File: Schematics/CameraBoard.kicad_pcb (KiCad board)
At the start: 4 copper layers, 50 x 100 mm, 72 parts, among them J1 Microsemi_FlashPro-JTAG-10, J2 USB_C_Receptacle, U1 STM32F405RGTx, U2 TPS22917DBVR, U3 TPS22917DBVR, U5 AMS1117-3.3, U6 TPS22917DBVR, U8 SN65HVD230, Y1 8mhz

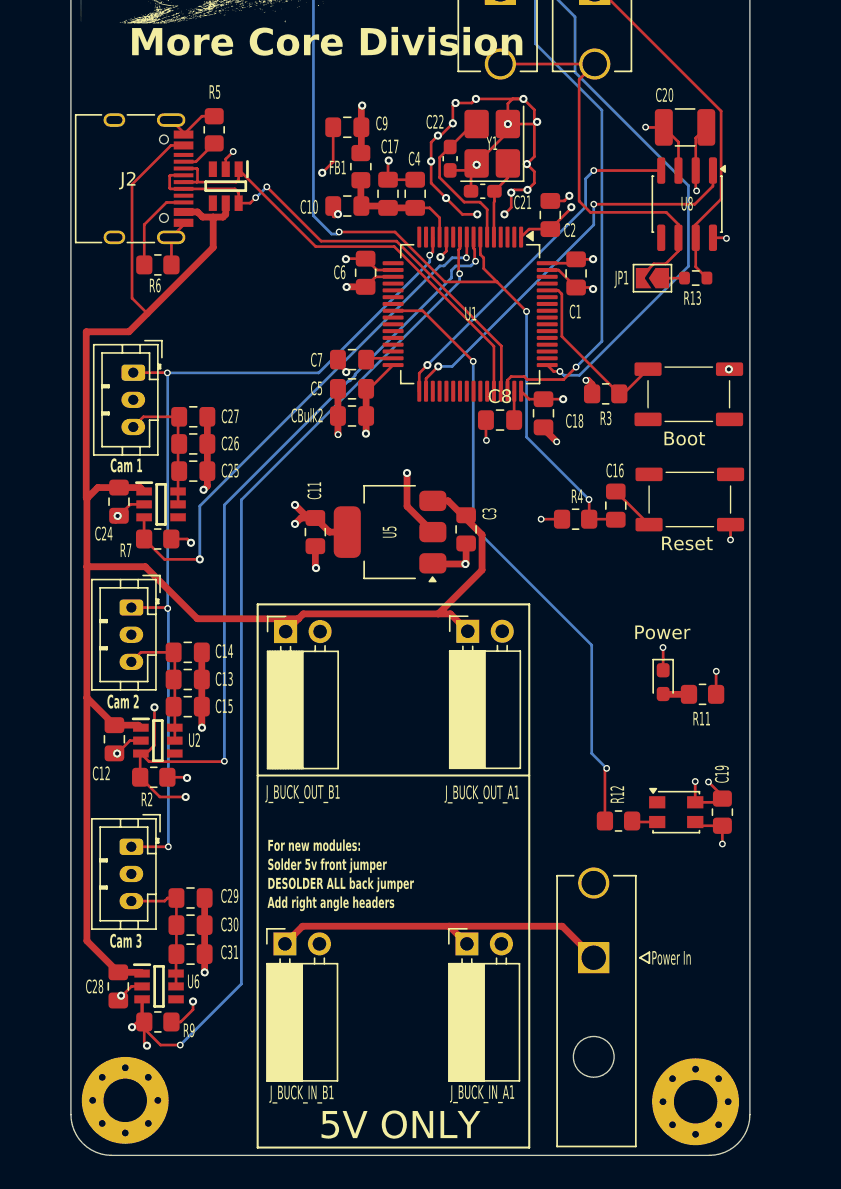
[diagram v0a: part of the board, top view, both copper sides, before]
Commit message: added LCSC numbers and generated BOM, fixed schematic
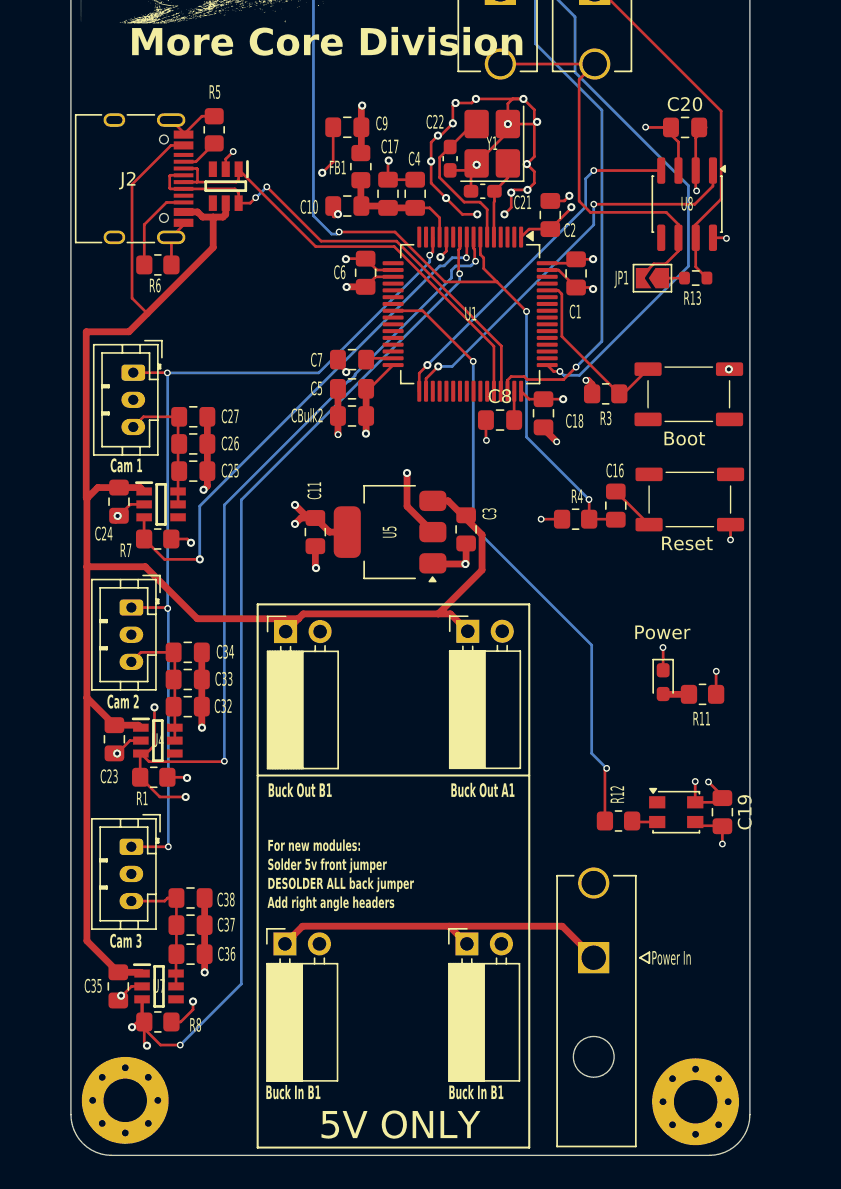
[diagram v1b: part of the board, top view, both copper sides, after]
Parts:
- removed C12, C14, C28, C29: 1u, Capacitor_SMD:C_0805_2012Metric_Pad1.18x1.45mm_HandSolder
- removed C13, C30: 47u, Capacitor_SMD:C_0805_2012Metric_Pad1.18x1.45mm_HandSolder
- removed C15, C31: .1u, Capacitor_SMD:C_0805_2012Metric_Pad1.18x1.45mm_HandSolder
- removed Cam1: Conn_01x03, Connector_JST:JST_PH_B3B-PH-K_1x03_P2.00mm_Vertical
- removed R2, R9: 100k, Resistor_SMD:R_0805_2012Metric_Pad1.20x1.40mm_HandSolder
- removed U2, U6: TPS22917DBVR, myFootprints:SOT95P280X145-6N
- added C23: 1uf, Capacitor_SMD:C_0805_2012Metric_Pad1.18x1.45mm_HandSolder, F.Cu at (74.7, 109.0)
- added C32: 1uf, Capacitor_SMD:C_0805_2012Metric_Pad1.18x1.45mm_HandSolder, F.Cu at (80.0, 106.6)
- added C33: 47uf, Capacitor_SMD:C_0805_2012Metric_Pad1.18x1.45mm_HandSolder, F.Cu at (80.0, 104.6)
- added C34: 100nf, Capacitor_SMD:C_0805_2012Metric_Pad1.18x1.45mm_HandSolder, F.Cu at (80.0, 102.6)
- added C35: 1uf, Capacitor_SMD:C_0805_2012Metric_Pad1.18x1.45mm_HandSolder, F.Cu at (74.9, 127.2)
- added C36: 1uf, Capacitor_SMD:C_0805_2012Metric_Pad1.18x1.45mm_HandSolder, F.Cu at (80.3, 124.8)
- added C37: 47uf, Capacitor_SMD:C_0805_2012Metric_Pad1.18x1.45mm_HandSolder, F.Cu at (80.3, 122.6)
- added C38: 100nf, Capacitor_SMD:C_0805_2012Metric_Pad1.18x1.45mm_HandSolder, F.Cu at (80.3, 120.6)
- added Cam2: Conn_01x03, Connector_JST:JST_PH_B3B-PH-K_1x03_P2.00mm_Vertical, F.Cu at (75.9, 99.3)
- added R1: 100kr, Resistor_SMD:R_0805_2012Metric_Pad1.20x1.40mm_HandSolder, F.Cu at (77.5, 111.8)
- added R8: 100kr, Resistor_SMD:R_0805_2012Metric_Pad1.20x1.40mm_HandSolder, F.Cu at (77.8, 129.8)
- added U4: TPS22917DBVR, myFootprints:SOT95P280X145-6N, F.Cu at (77.8, 109.1)
- added U7: TPS22917DBVR, myFootprints:SOT95P280X145-6N, F.Cu at (77.9, 127.2)
- C11: value 33u -> 33uf
- C17, C3, C9: value 1u -> 1uf
- C19: footprint Resistor_SMD:R_0805_2012Metric_Pad1.20x1.40mm_HandSolder -> Capacitor_SMD:C_0805_2012Metric_Pad1.18x1.45mm_HandSolder
- C20: value 100nF -> 100nf; footprint Capacitor_SMD:C_1210_3225Metric_Pad1.33x2.70mm_HandSolder -> Capacitor_SMD:C_0805_2012Metric_Pad1.18x1.45mm_HandSolder
- C7, C8: value 2.2u -> 2.2uf
- CAN_IN1, CAN_OUT1, PowerIn1: value ~ -> 2 pin Molex
- CBulk2: value 4.7u -> 4.7uf
- R11: value 1k -> 1kr
- R12: value .33k -> 330r
- R13: value 120R -> 120r
- R3: value 100k -> 100kr
- R4: value 10k -> 10kr
- R5, R6: value 5.1k -> 5.1kr
- U1: value STM32F405RGTx -> STM32F405RGT6
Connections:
- U1 pad 10: /Camera_center/CAM_C_PWN_EN -> /MCU/CAM_C_PWN_EN
- U1 pad 8: /Camera_left/CAM_L_PWN_EN -> /MCU/CAM_L_PWN_EN
- U1 pad 9: /Camera_right/CAM_R_PWN_EN -> /MCU/CAM_R_PWN_EN
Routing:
- net /MCU/CAM_L_PWN_EN: track 0.00 -> 63.7 mm, vias 0 -> 4
- net /Camera_left/CAM_L_PWN_EN: track 63.7 -> 0.00 mm, vias 4 -> 0
- net /Camera_right/<NO NET>: track 10.2 -> 20.0 mm
- net /Camera_left/<NO NET>: track 9.81 -> 0.00 mm
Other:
- board text added: "Buck In B1"
- board text added: "Buck Out A1"
- board text added: "Buck Out B1"

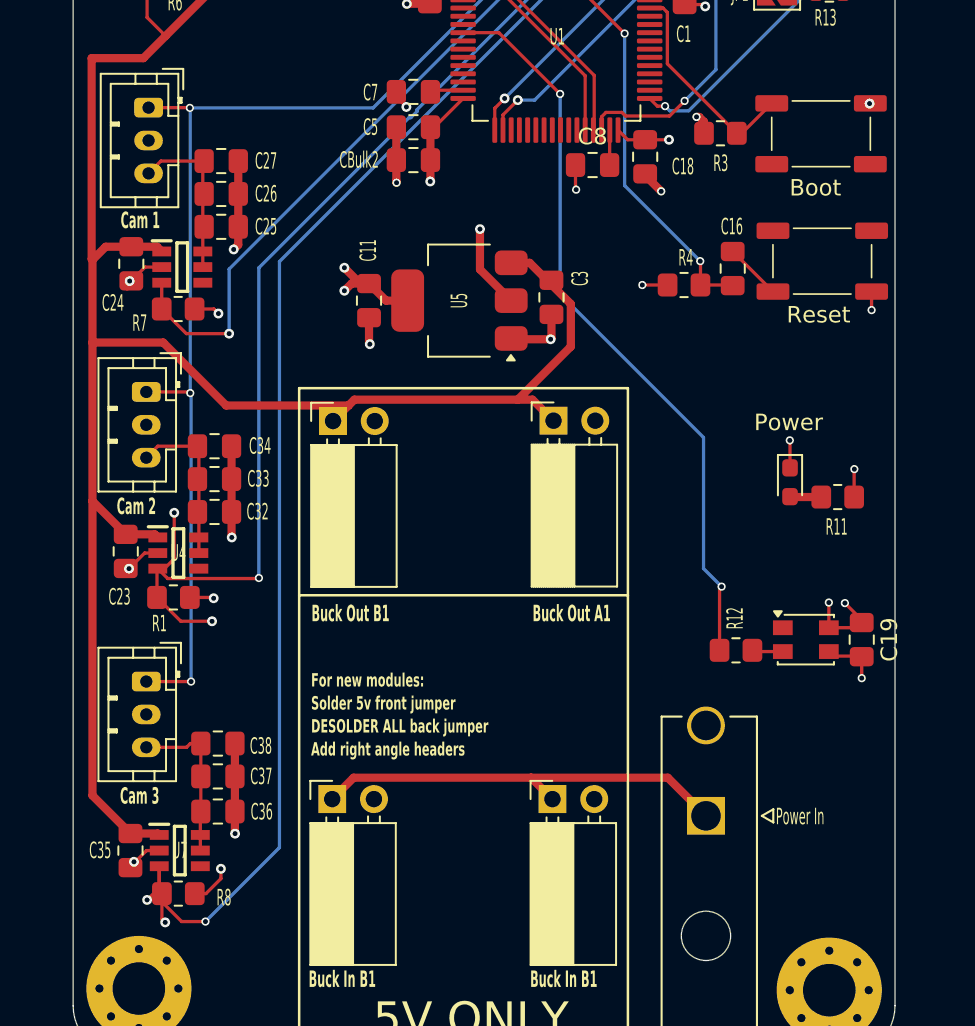
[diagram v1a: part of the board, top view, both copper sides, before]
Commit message: fixed switch layout and unrouted nets
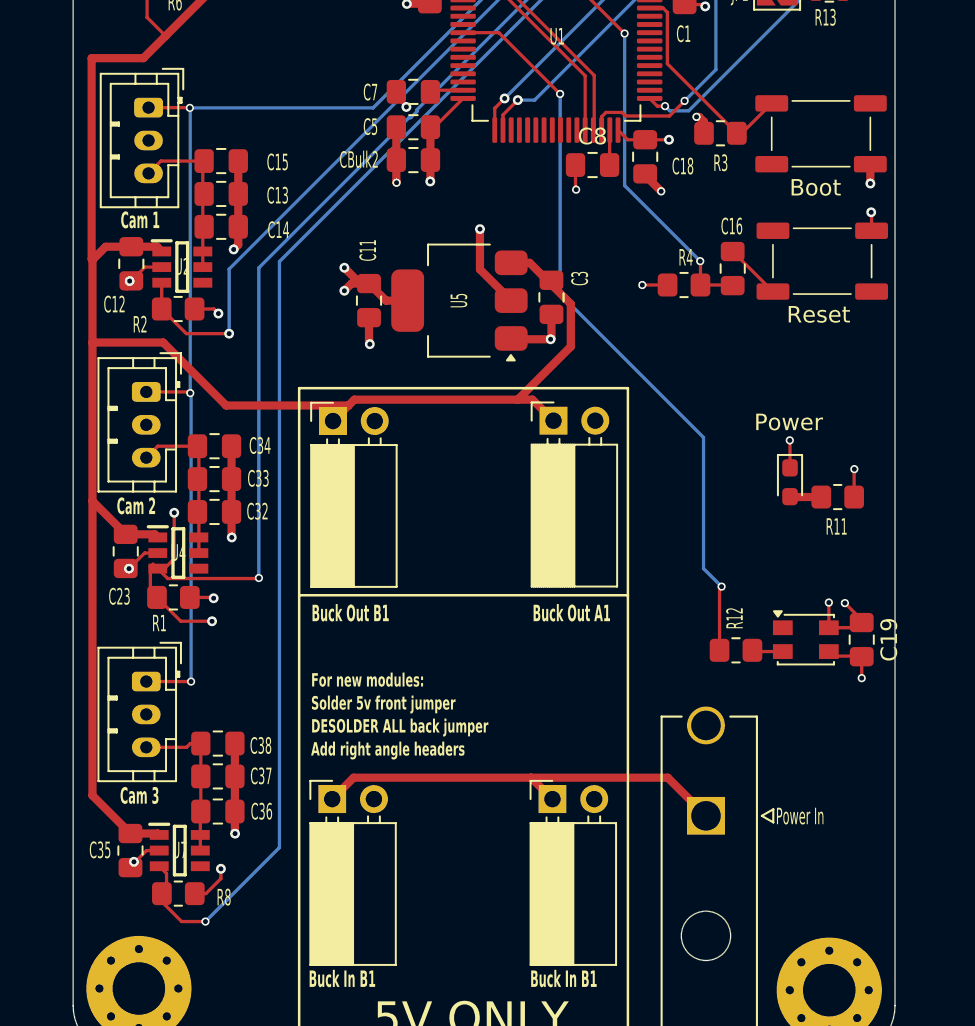
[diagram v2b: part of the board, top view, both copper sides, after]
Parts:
- removed C24, C25: 1u, Capacitor_SMD:C_0805_2012Metric_Pad1.18x1.45mm_HandSolder
- removed C26: 47u, Capacitor_SMD:C_0805_2012Metric_Pad1.18x1.45mm_HandSolder
- removed C27: .1u, Capacitor_SMD:C_0805_2012Metric_Pad1.18x1.45mm_HandSolder
- removed the Cam2 at (76.0, 82.0)
- removed R7: 100k, Resistor_SMD:R_0805_2012Metric_Pad1.20x1.40mm_HandSolder
- removed U3: TPS22917DBVR, myFootprints:SOT95P280X145-6N
- added C12: 1uf, Capacitor_SMD:C_0805_2012Metric_Pad1.18x1.45mm_HandSolder, F.Cu at (75.0, 91.5)
- added C13: 47uf, Capacitor_SMD:C_0805_2012Metric_Pad1.18x1.45mm_HandSolder, F.Cu at (80.5, 87.2)
- added C14: 1uf, Capacitor_SMD:C_0805_2012Metric_Pad1.18x1.45mm_HandSolder, F.Cu at (80.5, 89.2)
- added C15: 100nf, Capacitor_SMD:C_0805_2012Metric_Pad1.18x1.45mm_HandSolder, F.Cu at (80.5, 85.2)
- added Cam1: Conn_01x03, Connector_JST:JST_PH_B3B-PH-K_1x03_P2.00mm_Vertical, F.Cu at (76.0, 82.0)
- added R2: 100kr, Resistor_SMD:R_0805_2012Metric_Pad1.20x1.40mm_HandSolder, F.Cu at (77.8, 94.2)
- added U2: TPS22917DBVR, myFootprints:SOT95P280X145-6N, F.Cu at (78.1, 91.7)
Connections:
- BootSwitch1 pad 1: unconnected-(BootSwitch1-Pad1) -> +3.3V
- BootSwitch1 pad 3: +3.3V -> unconnected-(BootSwitch1-Pad3)
- RSTSwitch2 pad 1: GND -> unconnected-(RSTSwitch2-Pad1)
- RSTSwitch2 pad 3: unconnected-(RSTSwitch2-Pad3) -> GND
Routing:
- net /Camera_center/CAM_C_PWN_EN: track 77.7 -> 0.00 mm, vias 4 -> 0
- net (no net): track 0.00 -> 72.0 mm, vias 0 -> 2
- net /Camera_right/<NO NET>: track 20.0 -> 9.81 mm
- net /Camera_left/<NO NET>: track 0.00 -> 10.2 mm
- net /Camera_right/PWN_EN: track 0.00 -> 6.67 mm, vias 0 -> 1
- net /MCU/CAM_L_PWN_EN: track 63.7 -> 57.6 mm, vias 4 -> 3
- net /Camera_right/CAM_R_PWN_EN: track 39.0 -> 37.4 mm
- net /Camera_center/PWN_EN: track 0.00 -> 1.57 mm
- net /Camera_left/PWN_EN: track 0.00 -> 1.20 mm
- net +3.3V: track 55.6 -> 56.7 mm

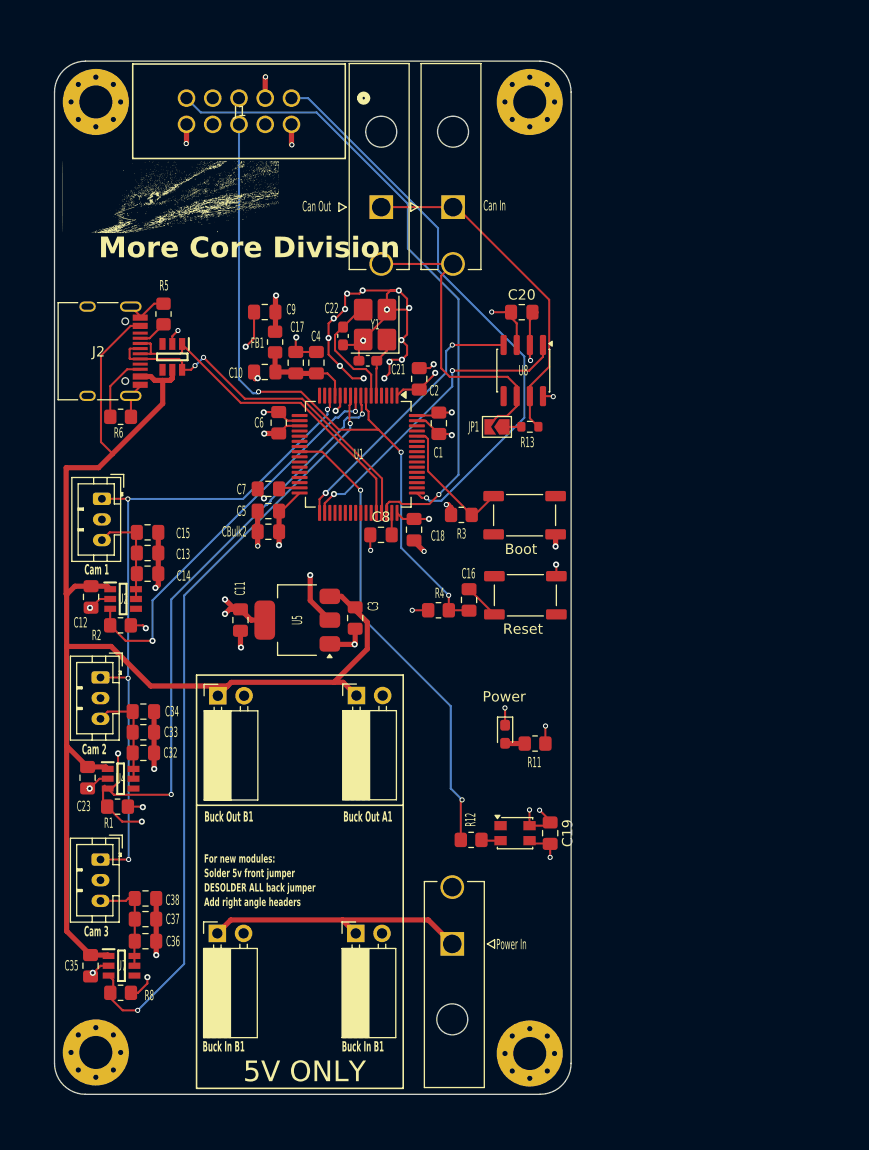
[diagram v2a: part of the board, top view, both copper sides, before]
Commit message: ran DRC, passed awaiting final review
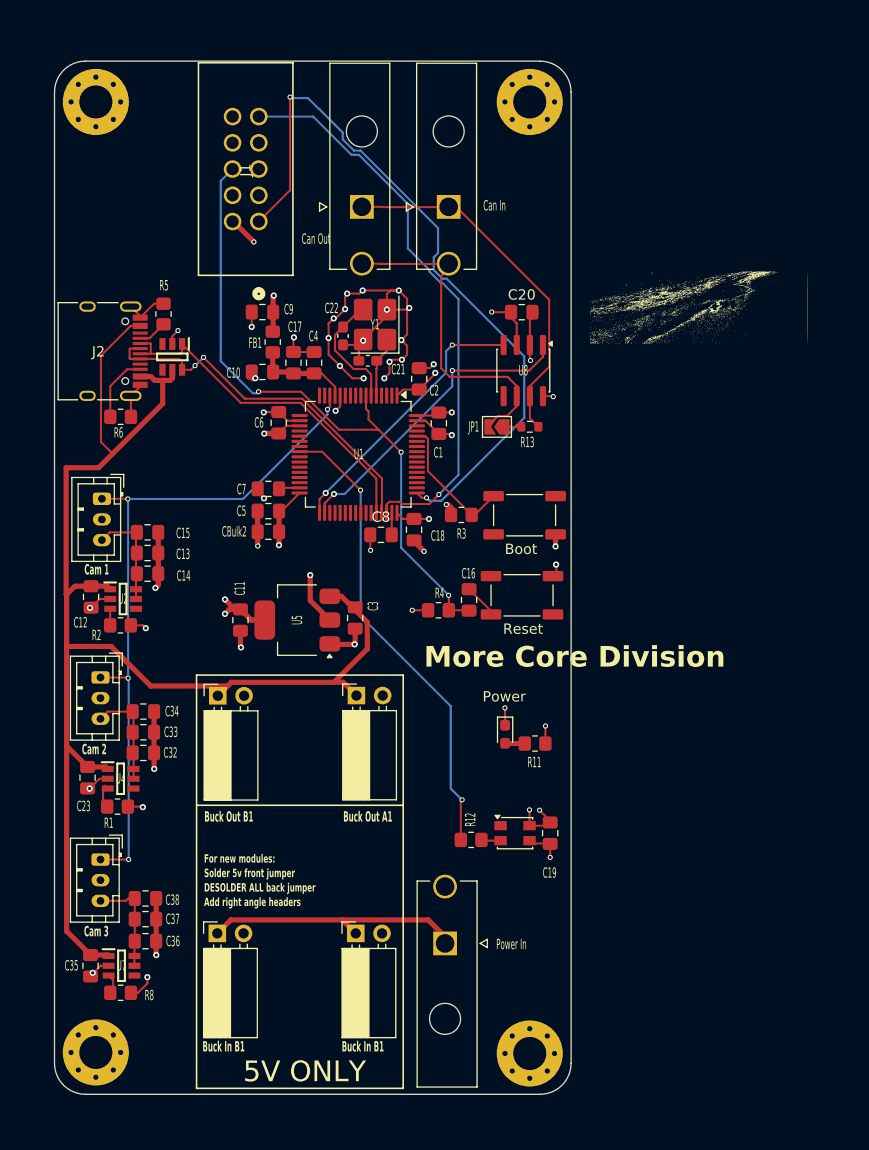
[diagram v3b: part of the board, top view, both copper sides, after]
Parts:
- moved G*** 52.3 mm to (133.8, 63.5), turned to 180 degrees
- moved J1 12.4 mm to (91.2, 55.1), turned to 90 degrees
- moved CAN_OUT1 1.88 mm to (101.2, 53.7)
- moved PowerIn1 0.70 mm to (109.2, 125.0)
- moved CAN_IN1 0.43 mm to (109.6, 53.7)
- moved RSTSwitch2 0.33 mm to (116.7, 91.3)
- moved C10 0.22 mm to (91.6, 69.7)
- moved C17 0.22 mm to (94.6, 68.8)
- moved C4 0.22 mm to (96.6, 68.8)
- moved C9 0.22 mm to (91.6, 63.9)
- moved FB1 0.22 mm to (92.6, 66.8)
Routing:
- net (no net): track 72.0 -> 0.00 mm, vias 2 -> 0
- net /MCU/CAM_L_PWN_EN: track 57.6 -> 0.00 mm, vias 3 -> 0
- net /Camera_right/CAM_R_PWN_EN: track 37.4 -> 0.00 mm, vias 2 -> 0
- net /MCU/SWCLK: track 55.3 -> 69.7 mm, vias 1 -> 2
- net /MCU/SWDIO: track 63.1 -> 55.4 mm
- net GND: track 126.6 -> 119.3 mm, vias 44 -> 42
- net /Camera_right/PWN_EN: track 6.67 -> 2.27 mm, vias 1 -> 0
- net /MCU/NRST: track 66.4 -> 63.3 mm
- net /Can_transceiver/CANL: track 31.1 -> 33.0 mm
- net /Can_transceiver/CANH: track 33.4 -> 35.3 mm
- net +3.3V: track 56.7 -> 57.6 mm

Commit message: final design pcb
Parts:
- removed the C11 at (89.5, 93.7)
- removed the C3 at (100.5, 93.5)
- removed G***: LOGO, LOGO
- removed the U5 at (95.0, 93.7)
- added C16: 1u, Capacitor_SMD:C_0805_2012Metric_Pad1.18x1.45mm_HandSolder, F.Cu at (93.0, 90.1)
- added C17: 4.7u, Capacitor_SMD:C_0805_2012Metric_Pad1.18x1.45mm_HandSolder, F.Cu at (103.9, 91.4)
- added D2: D_Schottky, Diode_SMD:D_2114_3652Metric, F.Cu at (90.8, 96.2)
- added D3: D_Schottky, Diode_SMD:D_2114_3652Metric, F.Cu at (88.0, 89.4)
- added U2: LDL1117-3.3, myFootprints:SOT230P700X180-4N, F.Cu at (98.5, 91.7)
- moved PowerIn1 0.63 mm to (109.3, 124.4)
- moved REF** 0.10 mm to (117.5, 135.6)
- renumbered C19 to C1, C18 to C10, C1 to C11, C17 to C12, C4 to C13, C21 to C14, C22 to C15, C12 to C18, C14 to C19, C16 to C2, C13 to C20, C15 to C21, C20 to C22, C32 to C24, C33 to C25, C34 to C26, C35 to C27, C36 to C28, C37 to C29, C7 to C3, C38 to C30, C8 to C4, C2 to C7, C9 to C8, C10 to C9, CBulk2 to CBulk1, D3 to D1, D1 to D4, R4 to R1, R8 to R10, R3 to R2, R11 to R3, R12 to R4, R2 to R5, R13 to R6, R6 to R7, R5 to R8, R1 to R9, RSTSwitch2 to RSTSwitch1, U2 to U3, U8 to U4, U4 to U5, U7 to U6
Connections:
- D4 pad 5: +5V -> /MCU/VBUS
- J2 pad A4: +5V -> /MCU/VBUS
- J2 pad A9: +5V -> /MCU/VBUS
- J2 pad B4: +5V -> /MCU/VBUS
- J2 pad B9: +5V -> /MCU/VBUS
- J_BUCK_IN_A1 pad 1: /Power/VBAT -> GND
- J_BUCK_IN_B1 pad 1: /Power/VBAT -> +BATT
- J_BUCK_IN_B1 pad 2: GND -> +BATT
- J_BUCK_OUT_A1 pad 1: +5V -> GND
- J_BUCK_OUT_B1 pad 2: GND -> +5V
- PowerIn1 pad 1: /Power/VBAT -> +BATT
- U1 pad 10: /MCU/CAM_C_PWN_EN -> /Camera_center/PWN_EN
- U1 pad 42: unconnected-(U1-PA9-Pad42) -> /MCU/VBUS
- U1 pad 8: /MCU/CAM_L_PWN_EN -> /Camera_left/PWN_EN
- U1 pad 9: /MCU/CAM_R_PWN_EN -> /Camera_right/PWN_EN
- U3 pad 5: /Camera_left/<NO NET> -> unconnected-(U3-QOD-Pad5)
- U5 pad 5: /Camera_right/<NO NET> -> unconnected-(U5-QOD-Pad5)
- U6 pad 5: /Camera_center/<NO NET> -> unconnected-(U6-QOD-Pad5)
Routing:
- net /Camera_center/PWN_EN: track 1.57 -> 74.1 mm, vias 0 -> 2
- net +5V: track 136.3 -> 67.7 mm
- net /MCU/VBUS: track 0.00 -> 57.7 mm
- net /Camera_right/PWN_EN: track 2.27 -> 58.5 mm, vias 0 -> 2
- net +BATT: track 0.00 -> 52.5 mm
- net /Camera_left/PWN_EN: track 1.20 -> 41.1 mm, vias 0 -> 2
- net /Power/VBAT: track 26.1 -> 0.00 mm
- net Net-(D2-K): track 0.00 -> 13.5 mm
- net +3.3V: track 57.6 -> 63.0 mm, vias 18 -> 17
- net /MCU/SWCLK: track 69.7 -> 64.8 mm
- net /Can_transceiver/CAN_RX_2: track 26.5 -> 28.2 mm
- net /Can_transceiver/CAN_TX_2: track 30.0 -> 31.6 mm
- net /MCU/RGB_DATA: track 45.4 -> 46.4 mm
- net /Camera_right/<NO NET>: track 9.81 -> 8.86 mm
- net /Camera_center/<NO NET>: track 9.94 -> 8.99 mm
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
